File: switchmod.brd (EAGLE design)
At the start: 42 x 43 mm, 38 parts, among them IC2 REG1117, U1 STM32F10XRXT6, X1 USB-MICROB

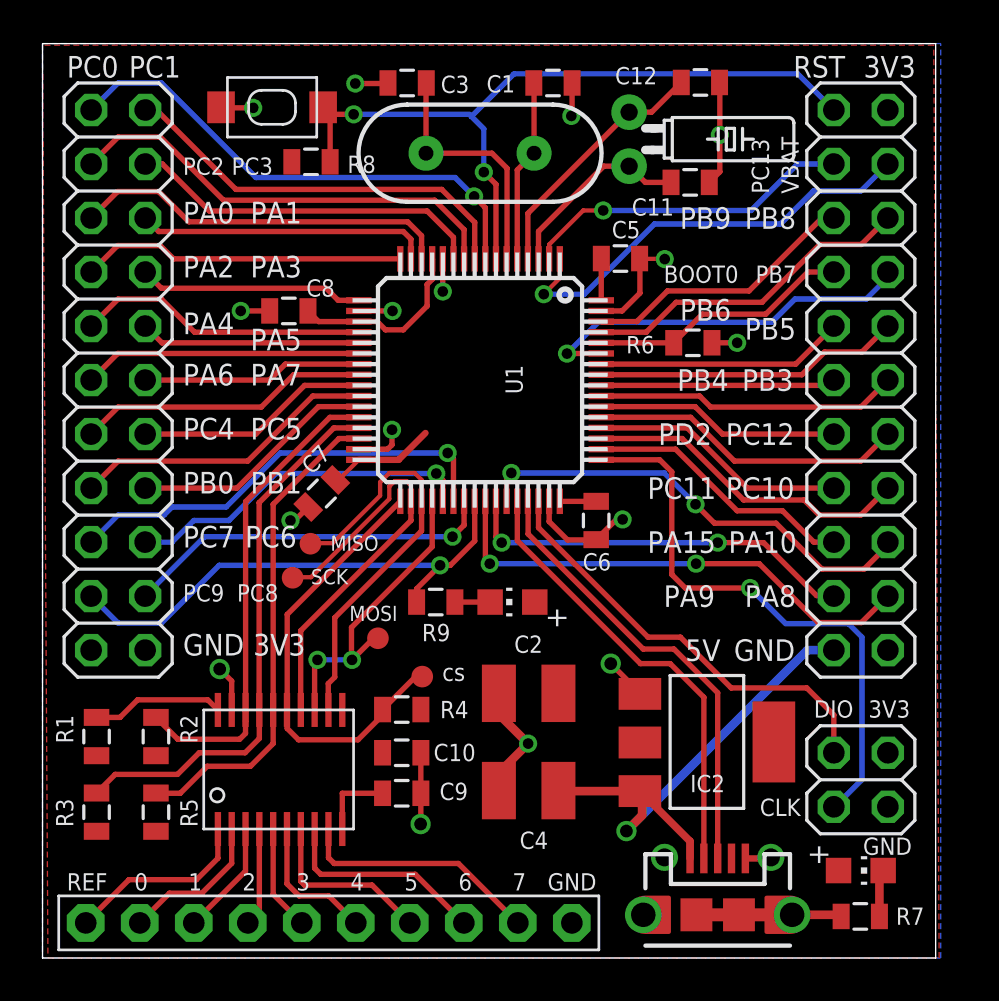
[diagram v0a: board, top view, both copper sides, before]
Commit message: adjusted header so they line up with 0.1in grid
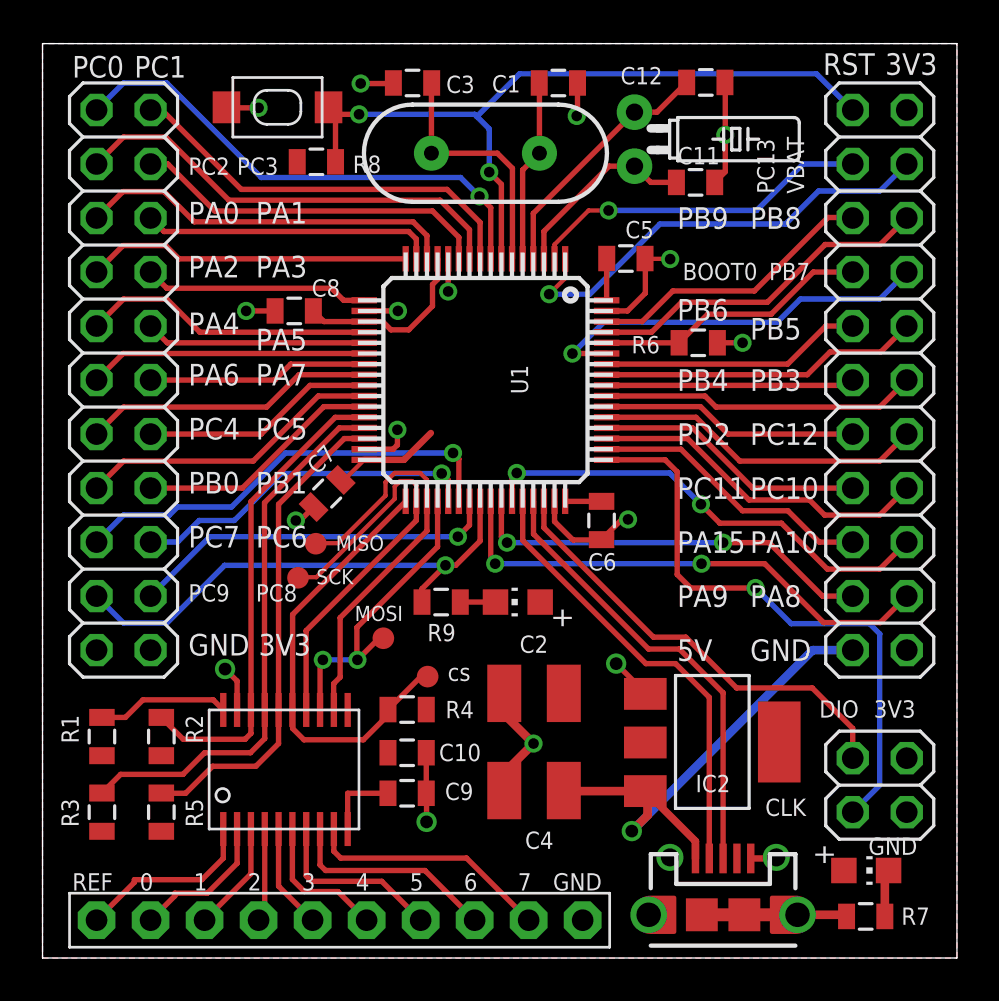
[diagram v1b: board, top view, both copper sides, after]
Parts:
- moved JP4 0.92 mm to (39.4, 8.13)
- moved JP2 0.89 mm to (39.4, 27.2)
- moved U$2 0.52 mm to (14.0, 1.78)
- moved R7 0.25 mm to (38.7, 1.96)
- moved C1 0.25 mm to (24.3, 41.1)
- moved C10 0.25 mm to (17.1, 9.65)
- moved C11 0.25 mm to (30.7, 36.5)
- moved C2 0.25 mm to (23.1, 12.4)
- moved C3 0.25 mm to (17.4, 41.1)
- moved C4 0.25 mm to (23.1, 7.87)
- moved C6 0.25 mm to (26.3, 20.6)
- moved C9 0.25 mm to (17.1, 7.75)
- moved LED2 0.25 mm to (22.4, 16.7)
- moved R4 0.25 mm to (17.1, 11.7)
- moved R8 0.25 mm to (12.9, 37.4)
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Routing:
- net N$22: track 27.1 -> 28.0 mm
- net N$63: track 20.9 -> 21.5 mm
- net N$58: track 14.4 -> 15.1 mm
- net N$61: track 15.7 -> 16.3 mm
- net N$59: track 11.7 -> 12.3 mm
- net N$57: track 11.0 -> 11.7 mm
- net N$55: track 11.5 -> 12.1 mm
- net N$54: track 12.1 -> 12.7 mm
- net N$51: track 12.7 -> 13.4 mm
- net N$33: track 18.7 -> 19.4 mm
- net N$26: track 12.3 -> 13.0 mm
- net N$64: track 15.6 -> 16.3 mm
- net N$62: track 13.0 -> 13.6 mm
- net N$66: track 23.3 -> 24.0 mm
- net N$56: track 14.2 -> 14.9 mm
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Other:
- board size 42 x 43 mm -> 43 x 43 mm

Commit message: board cleanup
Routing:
- net GND: track 50.2 -> 49.0 mm
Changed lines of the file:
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@@
 <text x="1.397" y="41.402" size="1.016" layer="25">PC0</text>
 <text x="4.318" y="41.402" size="1.016" layer="25">PC1</text>
-<text x="19.05" y="13.0302" size="0.8128" layer="25">cs</text>
+<text x="16.129" y="13.2842" size="0.8128" layer="25">cs</text>
 <text x="14.6812" y="15.8496" size="0.7112" layer="25">MOSI</text>
 <text x="13.7922" y="19.1516" size="0.7112" layer="25">MISO</text>
@@
 <wire x1="34.454" y1="4.682" x2="34.504" y2="4.732" width="0.254" layer="1"/>
 <via x="26.9748" y="13.843" extent="1-16" drill="0.6"/>
-<via x="23.0886" y="10.0838" extent="1-16" drill="0.5"/>
+<via x="21.6916" y="10.0838" extent="1-16" drill="0.5"/>
 <via x="8.5852" y="13.589" extent="1-16" drill="0.6"/>
 <contactref element="C10" pad="2"/>
@@
 <wire x1="8.5852" y1="13.589" x2="9.15" y2="13.0242" width="0.254" layer="1"/>
 <wire x1="9.15" y1="13.0242" x2="9.15" y2="11.665" width="0.254" layer="1"/>
-<wire x1="21.6378" y1="12.3698" x2="21.714" y2="12.446" width="0.254" layer="1"/>
 <wire x1="15.128" y1="23.928" x2="16.4858" y2="23.928" width="0.254" layer="1"/>
 <wire x1="16.4858" y1="23.928" x2="16.6878" y2="24.13" width="0.254" layer="1"/>
@@
 <wire x1="11.9126" y1="20.574" x2="12.1158" y2="20.574" width="0.254" layer="1"/>
 <wire x1="12.1158" y1="20.574" x2="12.749403125" y2="21.207603125" width="0.254" layer="1"/>
-<wire x1="21.714" y1="7.874" x2="21.714" y2="8.7092" width="0.4064" layer="1"/>
-<wire x1="21.714" y1="8.7092" x2="23.0886" y2="10.0838" width="0.4064" layer="1"/>
-<wire x1="21.6378" y1="12.3698" x2="21.6378" y2="11.5346" width="0.4064" layer="1"/>
-<wire x1="21.6378" y1="11.5346" x2="23.0886" y2="10.0838" width="0.4064" layer="1"/>
 <wire x1="18.0594" y1="6.4008" x2="18.0594" y2="7.7326" width="0.254" layer="1"/>
 <wire x1="18.0594" y1="7.7326" x2="18.045" y2="7.747" width="0.254" layer="1"/>
+<wire x1="21.6916" y1="10.0838" x2="21.6916" y2="12.446" width="0.4064" layer="1"/>
+<wire x1="21.6916" y1="12.446" x2="21.714" y2="12.446" width="0.4064" layer="1"/>
+<wire x1="21.6916" y1="10.0838" x2="21.6916" y2="7.874" width="0.4064" layer="1"/>
+<wire x1="21.6916" y1="7.874" x2="21.714" y2="7.874" width="0.4064" layer="1"/>
 </signal>
 <signal name="+3V3">
